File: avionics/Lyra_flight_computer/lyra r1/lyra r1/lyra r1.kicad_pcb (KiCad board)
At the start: 4 copper layers, 40 x 75 mm, 82 parts, among them J1 USB_B_Micro, J10 BOOT 0 HEADER, J11 Screw_Terminal_01x04, J12 Screw_Terminal_01x04, J2 UART Breakout, J3 Screw_Terminal_01x04, J4 I2C Breakout, J5 Screw_Terminal_01x04, J6 Conn_02x03_Top_Bottom, J7 Conn_02x03_Top_Bottom, J8 SPI Breakout, J9 MEM2067-02-180-00-A, Q1 AO3401A, Q2 Q_NMOS_GSD, Q3 Q_NMOS_GSD, SW1 SW_MEC_5E, SW2 SW_Push_DPDT, U1 LM317_SOT-223, U2 LM317_SOT-223, U3 USBLC6-2SC6, U4 BMI088, U5 BMP390L, U6 W25Q32JVSS, U7 STM32F405RGTx, X1 ECS-2520MV-xxx-xx

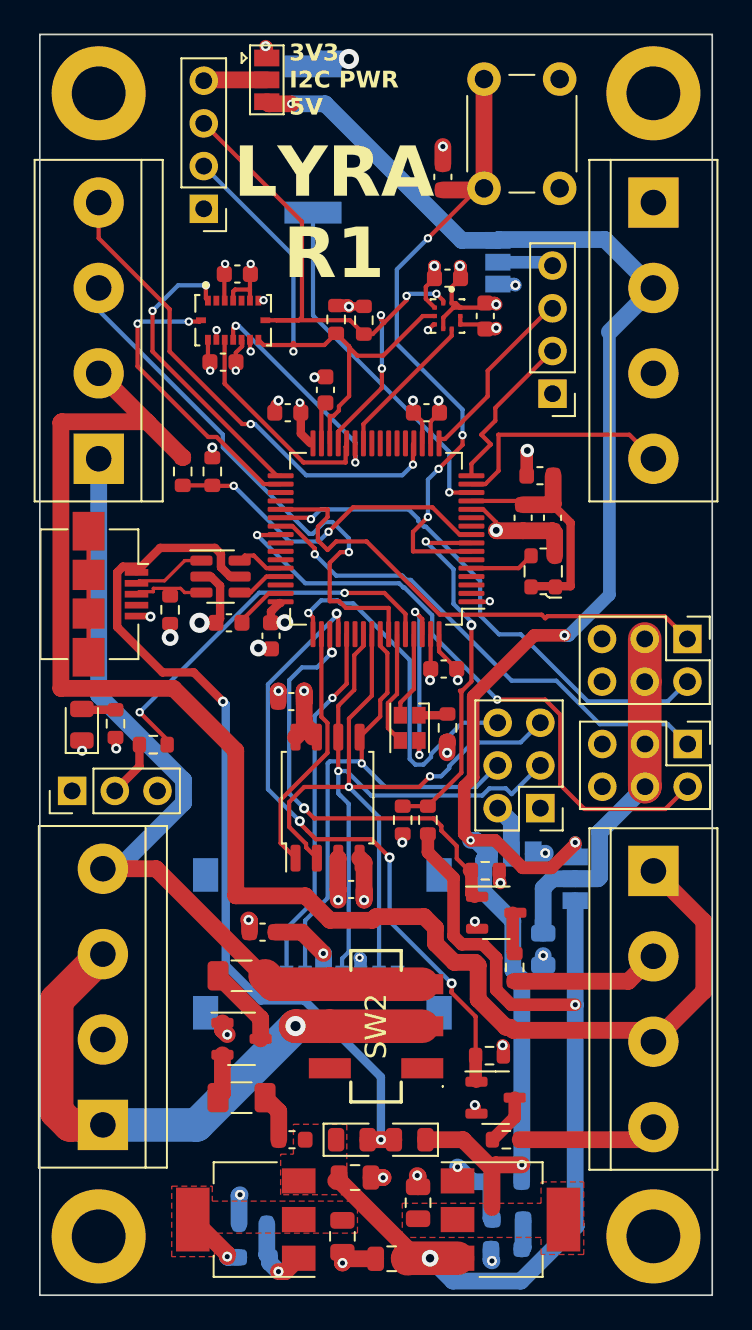
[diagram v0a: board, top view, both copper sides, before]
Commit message: lyra r1 redone with underneathdecoupling caps
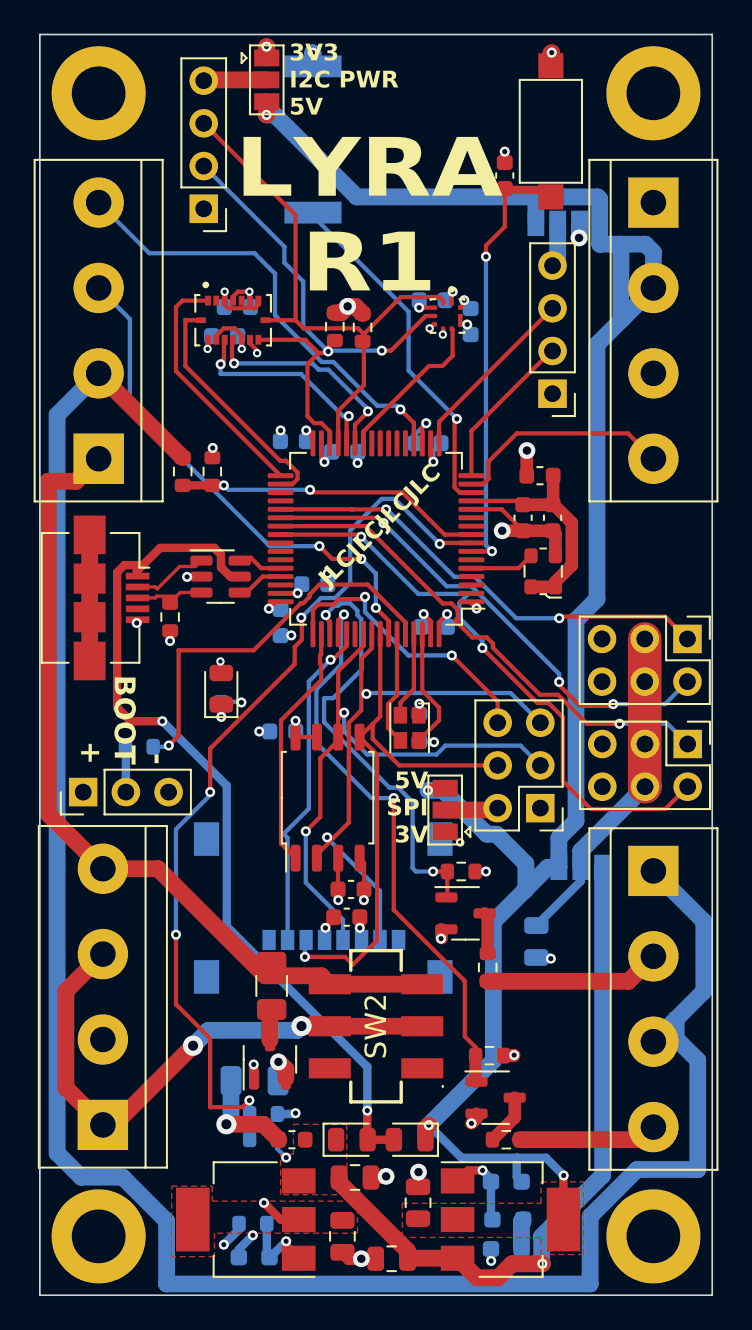
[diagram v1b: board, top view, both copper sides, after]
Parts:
- C10, C13, C14, C17, C20, C21, C22, C5, C6, C7, C8, F2, R11, R13, R14, R19, R7: moved to B.Cu
- JP3: moved to F.Cu
- SW1: value SW_MEC_5E -> SW_SPST; footprint Button_Switch_THT:SW_PUSH_6mm -> Button_Switch_SMD:SW_SPST_CK_RS282G05A3
- moved R13 21.4 mm to (138.6, 149.0), turned to 180 degrees
- moved R14 19.3 mm to (138.6, 147.5), turned to 0 degrees
- moved D3 8.56 mm to (136.0, 122.2)
- moved R11 6.64 mm to (136.0, 122.1)
- moved C14 5.60 mm to (141.6, 116.0), turned to 0 degrees
- moved C12 5.09 mm to (143.5, 135.8), turned to 180 degrees
- moved JP3 4.73 mm to (149.4, 129.4), turned to 90 degrees
- moved JP2 4.24 mm to (156.1, 94.5), turned to 180 degrees
- moved C13 3.86 mm to (143.4, 108.1), turned to 0 degrees
- moved C11 3.68 mm to (152.9, 91.6)
- moved SW1 3.15 mm to (155.7, 89.0)
- moved C20 2.57 mm to (148.7, 118.5)
- moved J9 2.13 mm to (142.1, 139.3)
- moved Q1 2.08 mm to (138.9, 144.2), turned to 90 degrees
- moved C5 1.97 mm to (137.0, 99.5)
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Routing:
- net ARM-: track 91.7 -> 125.3 mm
- net BATT SENSE: track 22.3 -> 53.9 mm, vias 2 -> 5
- net +12V: track 56.5 -> 41.8 mm
- net RESET: track 39.3 -> 25.8 mm, vias 4 -> 2
- net +5V: track 105.9 -> 118.2 mm, vias 5 -> 4
- net +3V3: track 48.3 -> 36.7 mm
- net GND: track 53.8 -> 43.9 mm, vias 34 -> 35
- net MISO: track 42.6 -> 33.2 mm
- net CS BRKOUT: track 21.6 -> 17.1 mm, vias 1 -> 2
- net SCL: track 37.2 -> 33.2 mm, vias 4 -> 0
- net LED RED: track 11.0 -> 7.23 mm, vias 2 -> 0
- net P2 EN: track 37.9 -> 34.5 mm, vias 4 -> 2
- net Net-(F2-Pad2): track 2.84 -> 6.20 mm, vias 0 -> 1
- net ACCEL INT1: track 17.8 -> 14.5 mm, vias 2 -> 0
- net ACCEL INT2: track 17.9 -> 14.7 mm, vias 2 -> 0
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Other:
- board text added: "- BOOT +"
- board text added: "3V3 UART PWR 5V"
- board text added: "5V SERVO 12V"
- board text added: "5V SPI 3V"
- board text added: "JLCJLCJLCJLC"
- board text removed: "I2C"
- board text removed: "SERVO"
- board text removed: "SPI"

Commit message: lyra work and exporting to jlcpcb
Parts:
- moved C11 2.96 mm to (153.7, 94.5), turned to 0 degrees
- moved SW1 1.34 mm to (154.3, 88.8)
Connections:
- J5 pad 1: +BATT -> +12P
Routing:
- net +12P: track 1.24 -> 53.3 mm, vias 1 -> 2
- net +BATT: track 49.8 -> 21.8 mm
- net +5V: track 118.2 -> 113.0 mm
- net CS SD: track 19.9 -> 22.4 mm
- net BATT SENSE: track 53.9 -> 52.0 mm
- net BATT PRESWITCH: track 35.1 -> 36.7 mm
- net VBUS: track 52.2 -> 53.7 mm
- net SERVO4: track 35.6 -> 34.2 mm
- net RESET: track 25.8 -> 24.7 mm
- net SERVO3: track 30.3 -> 29.6 mm
- net +3V3: track 36.7 -> 37.4 mm
- net GND: track 43.9 -> 44.6 mm
- net MOSI: track 34.2 -> 34.9 mm
